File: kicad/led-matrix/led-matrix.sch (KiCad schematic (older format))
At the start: 13 parts

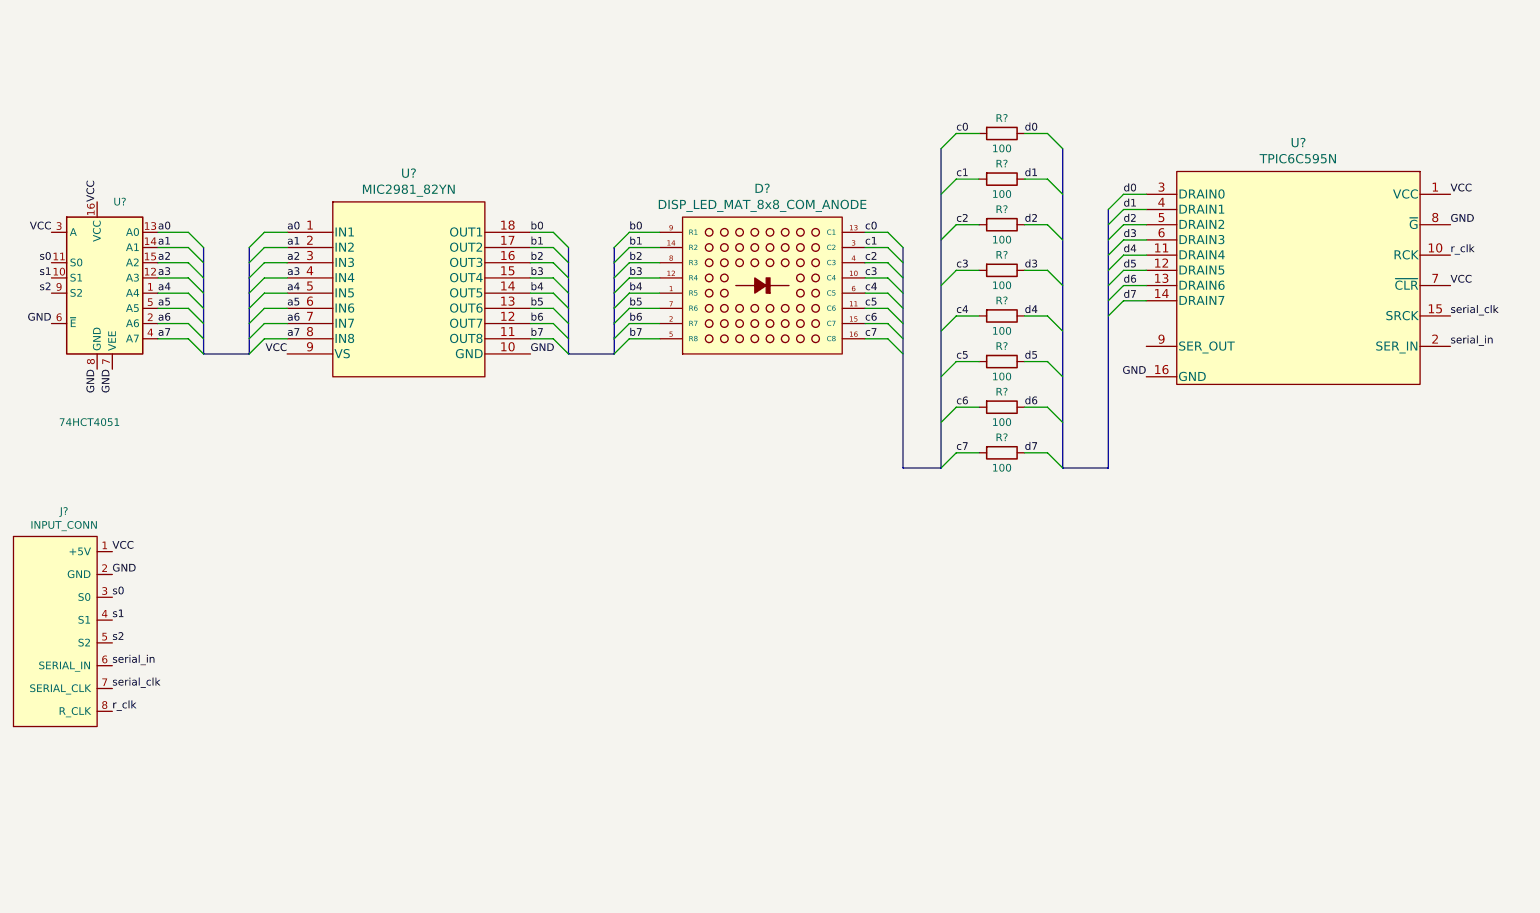
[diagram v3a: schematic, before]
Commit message: Finishes schematic
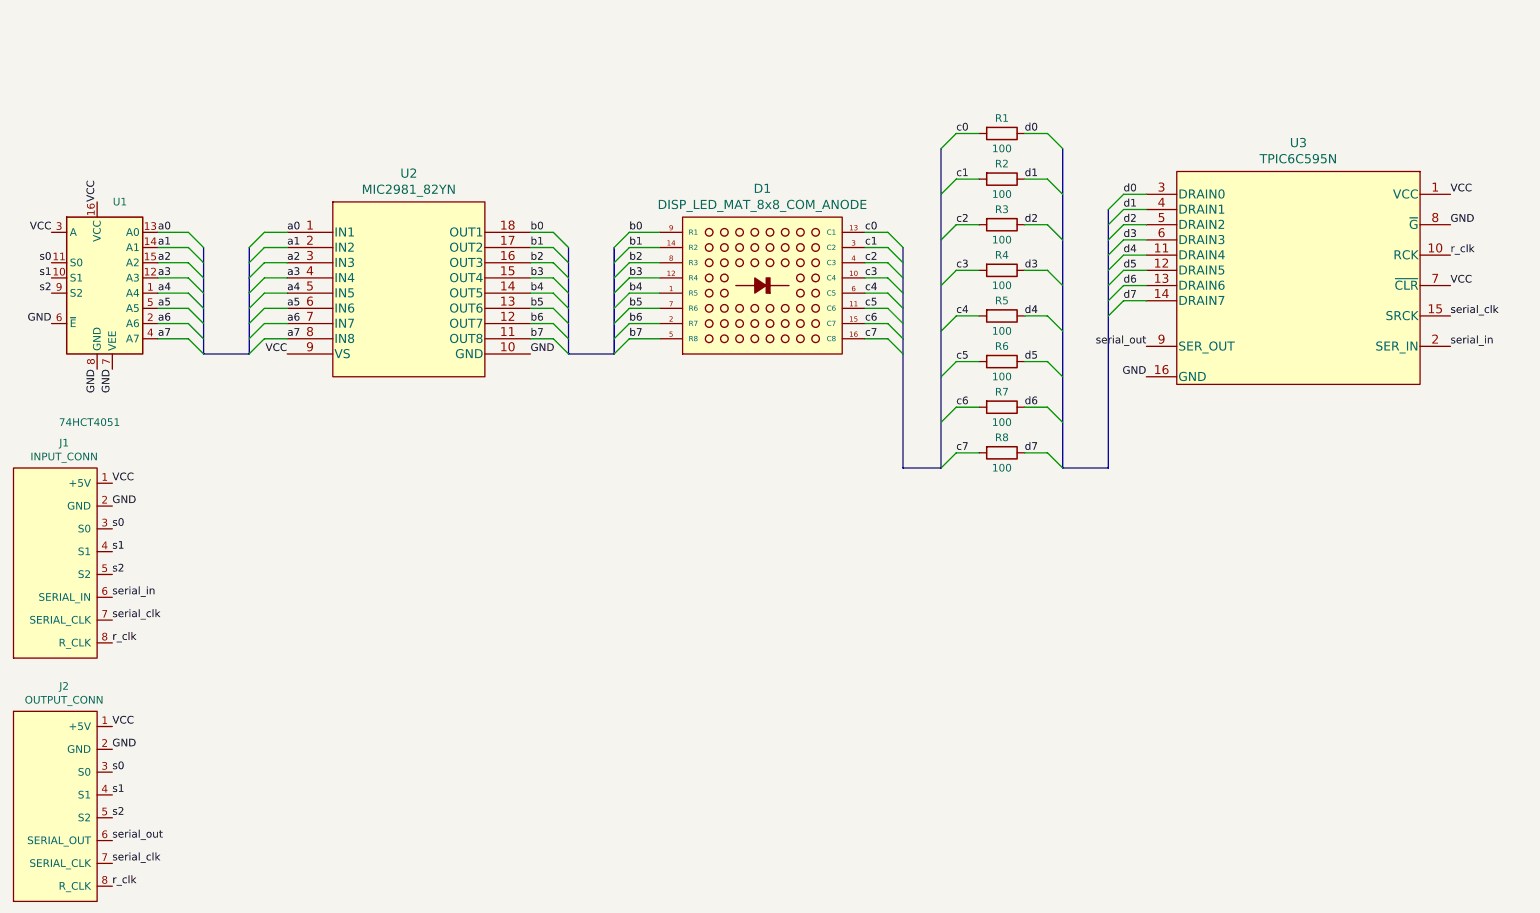
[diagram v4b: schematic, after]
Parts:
- removed J?: INPUT_CONN, symbol myConnectors:INPUT_CONN
- added J1: INPUT_CONN, Connector_PinHeader_2.00mm:PinHeader_1x08_P2.00mm_Vertical, symbol myConnectors:INPUT_CONN
- added J2: OUTPUT_CONN, Connector_PinHeader_2.00mm:PinHeader_1x08_P2.00mm_Vertical, symbol myConnectors:OUTPUT_CONN
- D1: renamed from D?; footprint (none) -> akn_misc:LED_8x8_3MM_32x32MM
- R1, R2, R3, R4, R5, R6, R7, R8: renamed from R?; footprint (none) -> Resistor_SMD:R_0603_1608Metric_Pad0.98x0.95mm_HandSolder
- U1: renamed from U?; footprint (none) -> footprints:DIP254P762X432-16P
- U2: renamed from U?; footprint PDIP18_N_MCH -> footprints:DIL18
- U3: renamed from U?; footprint N0016A -> footprints:TPIC6C595N
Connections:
- net GND: now also J1.2 (GND), J2.2 (GND)
- net VCC: now also J1.1 (+5V), J2.1 (+5V)
- net r_clk: now also J1.8 (R_CLK), J2.8 (R_CLK)
- net s0: now also J1.3 (S0), J2.3 (S0)
- net s1: now also J1.4 (S1), J2.4 (S1)
- net s2: now also J1.5 (S2), J2.5 (S2)
- net serial_clk: now also J1.7 (SERIAL_CLK), J2.7 (SERIAL_CLK)
- net serial_in: now also J1.6 (SERIAL_IN)
- net serial_out: now reaches U3.9 (SER_OUT)
- net serial_out: now also J2.6 (SERIAL_OUT)
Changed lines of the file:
@@
 	5050 1800 4850 1800
 $Comp
-L LED_MAT:DISP_LED_MAT_8x8_COM_ANODE D?
+L LED_MAT:DISP_LED_MAT_8x8_COM_ANODE D1
 U 1 1 5FD8261F
 P 5050 2600
-F 0 "D?" H 5725 3687 60  0000 C CNN
+F 0 "D1" H 5725 3687 60  0000 C CNN
 F 1 "DISP_LED_MAT_8x8_COM_ANODE" H 5725 3581 60  0000 C CNN
-F 2 "" H 5150 2550 60  0000 C CNN
+F 2 "akn_misc:LED_8x8_3MM_32x32MM" H 5150 2550 60  0001 C CNN
 F 3 "" H 5150 2550 60  0000 C CNN
 	1    5050 2600
@@
 	4200 2500 4350 2500
 $Comp
-L MIC2981:MIC2981_82YN U?
+L MIC2981:MIC2981_82YN U2
 U 1 1 5FD80D89
 P 2600 1800
-F 0 "U?" H 3400 2187 60  0000 C CNN
+F 0 "U2" H 3400 2187 60  0000 C CNN
 F 1 "MIC2981_82YN" H 3400 2081 60  0000 C CNN
-F 2 "PDIP18_N_MCH" H 3400 2040 60  0001 C CNN
+F 2 "footprints:DIL18" H 3400 2040 60  0001 C CNN
 F 3 "" H 2600 1800 60  0000 C CNN
 	1    2600 1800
@@
 VCC
 $Comp
-L TPIC6C595N:TPIC6C595N U?
+L TPIC6C595N:TPIC6C595N U3
 U 1 1 5FE09D0E
 P 9250 2150
-F 0 "U?" H 9250 3088 60  0000 C CNN
+F 0 "U3" H 9250 3088 60  0000 C CNN
 F 1 "TPIC6C595N" H 9250 2982 60  0000 C CNN
-F 2 "N0016A" H 9250 2090 60  0001 C CNN
+F 2 "footprints:TPIC6C595N" H 9250 2090 60  0001 C CNN
 F 3 "" H 9250 2150 60  0000 C CNN
 	1    9250 2150
@@
 Text Label 4200 2600 0    50   ~ 0
 GND
-Text Label 8250 2750 2    50   ~ 0
-GND
 Text Label 10250 1750 0    50   ~ 0
 GND
 $Comp
-L Device:R R?
+L Device:R R3
 U 1 1 5FE118EA
 P 7300 1750
-F 0 "R?" V 7200 1750 50  0000 C CNN
+F 0 "R3" V 7200 1750 50  0000 C CNN
 F 1 "100" V 7400 1750 50  0000 C CNN
-F 2 "" V 7230 1750 50  0001 C CNN
+F 2 "Resistor_SMD:R_0603_1608Metric_Pad0.98x0.95mm_HandSolder" V 7230 1750 50  0001 C CNN
 F 3 "~" H 7300 1750 50  0001 C CNN
 	1    7300 1750
@@
 $EndComp
 $Comp
-L Device:R R?
+L Device:R R4
 U 1 1 5FE13757
 P 7300 2050
-F 0 "R?" V 7200 2050 50  0000 C CNN
+F 0 "R4" V 7200 2050 50  0000 C CNN
 F 1 "100" V 7400 2050 50  0000 C CNN
-F 2 "" V 7230 2050 50  0001 C CNN
+F 2 "Resistor_SMD:R_0603_1608Metric_Pad0.98x0.95mm_HandSolder" V 7230 2050 50  0001 C CNN
 F 3 "~" H 7300 2050 50  0001 C CNN
 	1    7300 2050
@@
 $EndComp
 $Comp
-L Device:R R?
+L Device:R R5
 U 1 1 5FE13C09
 P 7300 2350
-F 0 "R?" V 7200 2350 50  0000 C CNN
+F 0 "R5" V 7200 2350 50  0000 C CNN
 F 1 "100" V 7400 2350 50  0000 C CNN
-F 2 "" V 7230 2350 50  0001 C CNN
+F 2 "Resistor_SMD:R_0603_1608Metric_Pad0.98x0.95mm_HandSolder" V 7230 2350 50  0001 C CNN
 F 3 "~" H 7300 2350 50  0001 C CNN
 	1    7300 2350
@@
 $EndComp
 $Comp
-L Device:R R?
+L Device:R R6
 U 1 1 5FE14227
 P 7300 2650
-F 0 "R?" V 7200 2650 50  0000 C CNN
+F 0 "R6" V 7200 2650 50  0000 C CNN
 F 1 "100" V 7400 2650 50  0000 C CNN
-F 2 "" V 7230 2650 50  0001 C CNN
+F 2 "Resistor_SMD:R_0603_1608Metric_Pad0.98x0.95mm_HandSolder" V 7230 2650 50  0001 C CNN
 F 3 "~" H 7300 2650 50  0001 C CNN
 	1    7300 2650
@@
 $EndComp
 $Comp
-L Device:R R?
+L Device:R R7
 U 1 1 5FE146EF
 P 7300 2950
-F 0 "R?" V 7200 2950 50  0000 C CNN
+F 0 "R7" V 7200 2950 50  0000 C CNN
 F 1 "100" V 7400 2950 50  0000 C CNN
-F 2 "" V 7230 2950 50  0001 C CNN
+F 2 "Resistor_SMD:R_0603_1608Metric_Pad0.98x0.95mm_HandSolder" V 7230 2950 50  0001 C CNN
 F 3 "~" H 7300 2950 50  0001 C CNN
 	1    7300 2950
@@
 $EndComp
 $Comp
-L Device:R R?
+L Device:R R2
 U 1 1 5FE14B19
 P 7300 1450
-F 0 "R?" V 7200 1450 50  0000 C CNN
+F 0 "R2" V 7200 1450 50  0000 C CNN
 F 1 "100" V 7400 1450 50  0000 C CNN
-F 2 "" V 7230 1450 50  0001 C CNN
+F 2 "Resistor_SMD:R_0603_1608Metric_Pad0.98x0.95mm_HandSolder" V 7230 1450 50  0001 C CNN
 F 3 "~" H 7300 1450 50  0001 C CNN
 	1    7300 1450
@@
 $EndComp
 $Comp
-L Device:R R?
+L Device:R R1
 U 1 1 5FE14FC7
 P 7300 1150
-F 0 "R?" V 7200 1150 50  0000 C CNN
+F 0 "R1" V 7200 1150 50  0000 C CNN
 F 1 "100" V 7400 1150 50  0000 C CNN
-F 2 "" V 7230 1150 50  0001 C CNN
+F 2 "Resistor_SMD:R_0603_1608Metric_Pad0.98x0.95mm_HandSolder" V 7230 1150 50  0001 C CNN
 F 3 "~" H 7300 1150 50  0001 C CNN
 	1    7300 1150
 	0    1    1    0
 $EndComp
-Text Label 1450 4050 0    50   ~ 0
+Text Label 1450 3600 0    50   ~ 0
 GND
 Text Label 1050 1800 2    50   ~ 0
 VCC
-Text Label 1450 3900 0    50   ~ 0
-VCC
-$Comp
-L 74xx:74HCT4051 U?
+$Comp
+L 74xx:74HCT4051 U1
 U 1 1 5FD7E6DB
 P 1350 2100
-F 0 "U?" H 1500 2600 50  0000 C CNN
+F 0 "U1" H 1500 2600 50  0000 C CNN
 F 1 "74HCT4051" H 1300 1150 50  0000 C CNN
-F 2 "" H 1350 1700 50  0001 C CNN
+F 2 "footprints:DIP254P762X432-16P" H 1350 1700 50  0001 C CNN
 F 3 "http://www.ti.com/lit/ds/symlink/cd74hct4051.pdf" H 1350 1700 50  0001 C CNN
 	1    1350 2100
@@
 c6
 $Comp
-L Device:R R?
+L Device:R R8
 U 1 1 5FE96CA4
 P 7300 3250
-F 0 "R?" V 7200 3250 50  0000 C CNN
+F 0 "R8" V 7200 3250 50  0000 C CNN
 F 1 "100" V 7400 3250 50  0000 C CNN
-F 2 "" V 7230 3250 50  0001 C CNN
+F 2 "Resistor_SMD:R_0603_1608Metric_Pad0.98x0.95mm_HandSolder" V 7230 3250 50  0001 C CNN
 F 3 "~" H 7300 3250 50  0001 C CNN
 	1    7300 3250
@@
 Text Label 1050 2400 2    50   ~ 0
 GND
-Text Label 1450 4200 0    50   ~ 0
+Text Label 1450 3750 0    50   ~ 0
 s0
 Text Label 1050 2000 2    50   ~ 0
 s0
-Text Label 1450 4350 0    50   ~ 0
+Text Label 1450 3900 0    50   ~ 0
 s1
-Text Label 1450 4500 0    50   ~ 0
+Text Label 1450 4050 0    50   ~ 0
 s2
 Text Label 1050 2100 2    50   ~ 0
@@
 Text Label 1050 2200 2    50   ~ 0
 s2
-Text Label 1450 4950 0    50   ~ 0
+Text Label 1450 4500 0    50   ~ 0
 r_clk
 Text Label 10250 1950 0    50   ~ 0
 r_clk
-Text Label 1450 4650 0    50   ~ 0
+Text Label 1450 4200 0    50   ~ 0
 serial_in
-Text Label 10250 2550 0    50   ~ 0
-serial_in
-Wire Bus Line
-	8000 1650 8000 3350
-Wire Bus Line
-	7700 1250 7700 3350
-Wire Bus Line
-	6900 1250 6900 3350
-Wire Bus Line
-	6650 1900 6650 3350
-Wire Bus Line
-	2050 1900 2050 2600
-Wire Bus Line
-	2350 1900 2350 2600
-Wire Bus Line
-	4450 1900 4450 2600
-Wire Bus Line
-	4750 1900 4750 2600
-$Comp
-L myConnectors:INPUT_CONN J?
-U 1 1 5FDA3D76
-P 1450 3750
-F 0 "J?" H 1133 3865 50  0000 C CNN
-F 1 "INPUT_CONN" H 1133 3774 50  0000 C CNN
-F 2 "" H 1450 3750 50  0001 C CNN
-F 3 "" H 1450 3750 50  0001 C CNN
-	1    1450 3750
-	1    0    0    -1
-$EndComp
-Text Label 1450 4800 0    50   ~ 0
+Text Label 1450 4350 0    50   ~ 0
 serial_clk
 Text Label 10250 2350 0    50   ~ 0
 serial_clk
+Text Label 8250 2550 2    50   ~ 0
+serial_out
+Text Label 1450 5800 0    50   ~ 0
+serial_out
+Text Label 1450 5050 0    50   ~ 0
+VCC
+Text Label 1450 5200 0    50   ~ 0
+GND
+Text Label 1450 5350 0    50   ~ 0
+s0
+Text Label 1450 5500 0    50   ~ 0
+s1
+Text Label 1450 5650 0    50   ~ 0
+s2
+Text Label 1450 5950 0    50   ~ 0
+serial_clk
+Text Label 1450 6100 0    50   ~ 0
+r_clk
+Text Label 10250 2550 0    50   ~ 0
+serial_in
+Text Label 8250 2750 2    50   ~ 0
+GND
+$Comp
+L myConnectors:INPUT_CONN J1
+U 1 1 5FE10ADF
+P 1450 3300
+F 0 "J1" H 1133 3415 50  0000 C CNN
+F 1 "INPUT_CONN" H 1133 3324 50  0000 C CNN
+F 2 "Connector_PinHeader_2.00mm:PinHeader_1x08_P2.00mm_Vertical" H 1450 3300 50  0001 C CNN
+F 3 "" H 1450 3300 50  0001 C CNN
+	1    1450 3300
+	1    0    0    -1
+$EndComp
+$Comp
+L myConnectors:OUTPUT_CONN J2
+U 1 1 5FE11788
+P 1450 4900
+F 0 "J2" H 1133 5015 50  0000 C CNN
+F 1 "OUTPUT_CONN" H 1133 4924 50  0000 C CNN
+F 2 "Connector_PinHeader_2.00mm:PinHeader_1x08_P2.00mm_Vertical" H 1450 4900 50  0001 C CNN
+F 3 "" H 1450 4900 50  0001 C CNN
+	1    1450 4900
+	1    0    0    -1
+$EndComp
+Text Label 1450 3450 0    50   ~ 0
+VCC
+Wire Bus Line
+	4750 1900 4750 2600
+Wire Bus Line
+	4450 1900 4450 2600
+Wire Bus Line
+	2350 1900 2350 2600
+Wire Bus Line
+	2050 1900 2050 2600
+Wire Bus Line
+	6900 1250 6900 3350
+Wire Bus Line
+	7700 1250 7700 3350
+Wire Bus Line
+	8000 1650 8000 3350
+Wire Bus Line
+	6650 1900 6650 3350
 $EndSCHEMATC

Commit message: Update schematic, pcb
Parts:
- U1: footprint footprints:DIP254P762X432-16P -> Package_DIP:DIP-16_W7.62mm
- U2: footprint footprints:DIL18 -> Package_DIP:DIP-18_W7.62mm
- U3: footprint footprints:TPIC6C595N -> Package_DIP:DIP-16_W7.62mm
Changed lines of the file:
@@
 F 0 "U2" H 3400 2187 60  0000 C CNN
 F 1 "MIC2981_82YN" H 3400 2081 60  0000 C CNN
-F 2 "footprints:DIL18" H 3400 2040 60  0001 C CNN
+F 2 "Package_DIP:DIP-18_W7.62mm" H 3400 2040 60  0001 C CNN
 F 3 "" H 2600 1800 60  0000 C CNN
 	1    2600 1800
@@
 F 0 "U3" H 9250 3088 60  0000 C CNN
 F 1 "TPIC6C595N" H 9250 2982 60  0000 C CNN
-F 2 "footprints:TPIC6C595N" H 9250 2090 60  0001 C CNN
+F 2 "Package_DIP:DIP-16_W7.62mm" H 9250 2090 60  0001 C CNN
 F 3 "" H 9250 2150 60  0000 C CNN
 	1    9250 2150
@@
 F 0 "U1" H 1500 2600 50  0000 C CNN
 F 1 "74HCT4051" H 1300 1150 50  0000 C CNN
-F 2 "footprints:DIP254P762X432-16P" H 1350 1700 50  0001 C CNN
+F 2 "Package_DIP:DIP-16_W7.62mm" H 1350 1700 50  0001 C CNN
 F 3 "http://www.ti.com/lit/ds/symlink/cd74hct4051.pdf" H 1350 1700 50  0001 C CNN
 	1    1350 2100
